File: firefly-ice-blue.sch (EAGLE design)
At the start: 119 parts, among them J1 USB-5PINMOLEX-47346, J2 CON-6SOCKET, U1 EFM32LG330F256, U10 STM6519, U11 TPS782XX, U12 TPS6208X, U13 NX3L1T53, U14 FDFMA2P029Z, U16 MEMORY-SPIWLBGA-8, U17 ADP151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

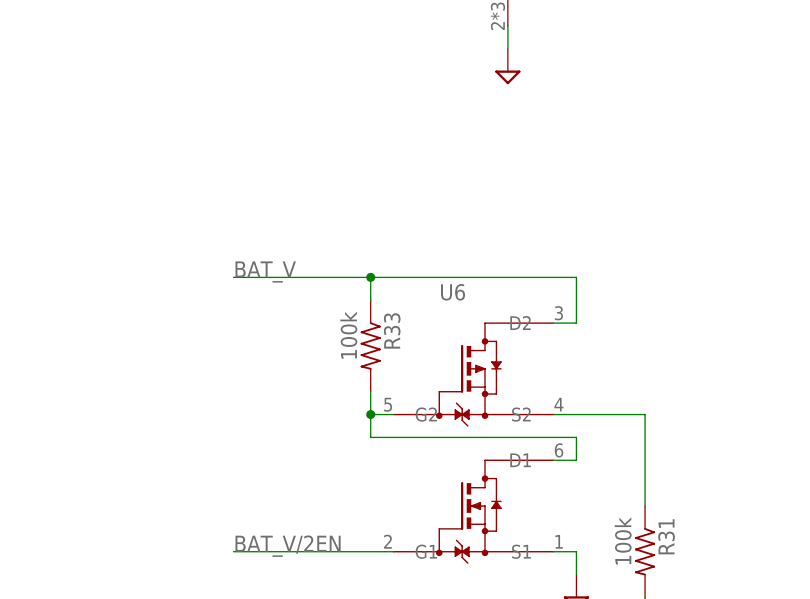
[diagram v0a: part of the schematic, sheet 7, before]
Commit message: fix reversed source/drain on p-channel mosfet of voltage sensing circuit
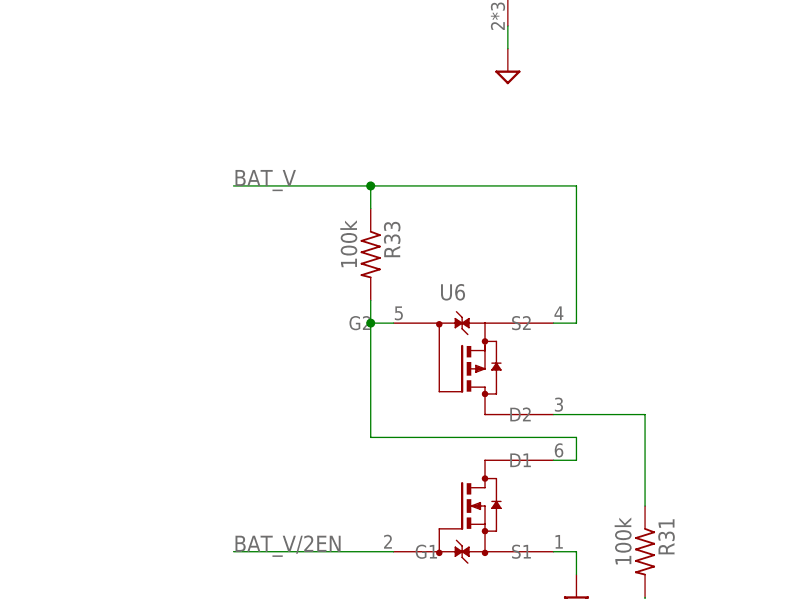
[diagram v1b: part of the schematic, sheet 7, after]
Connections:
- net BAT_V: now also U6.S2; no longer U6.D2
- net N$60: now also U6.D2; no longer U6.S2
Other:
- moved on the sheet: R33
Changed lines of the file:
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@@
 <attribute name="ORDERING-CODE" x="55.88" y="50.8" size="1.778" layer="96" display="off"/>
 </instance>
-<instance part="R33" gate="G$1" x="45.72" y="60.96" rot="R270">
-<attribute name="MANUFACTURER" x="45.72" y="60.96" size="1.778" layer="96" rot="R270" display="off"/>
-<attribute name="ORDERING-CODE" x="45.72" y="60.96" size="1.778" layer="96" rot="R270" display="off"/>
-<attribute name="VARIANTS" x="45.72" y="60.96" size="1.778" layer="96" rot="R270" display="off"/>
+<instance part="R33" gate="G$1" x="45.72" y="71.12" rot="R270">
+<attribute name="MANUFACTURER" x="45.72" y="71.12" size="1.778" layer="96" rot="R270" display="off"/>
+<attribute name="ORDERING-CODE" x="45.72" y="71.12" size="1.778" layer="96" rot="R270" display="off"/>
+<attribute name="VARIANTS" x="45.72" y="71.12" size="1.778" layer="96" rot="R270" display="off"/>
 </instance>
 <instance part="V93" gate="GND" x="68.58" y="33.02"/>
@@
 <segment>
 <pinref part="R33" gate="G$1" pin="1"/>
-<wire x1="45.72" y1="66.04" x2="45.72" y2="68.58" width="0.1524" layer="91"/>
-<wire x1="45.72" y1="68.58" x2="68.58" y2="68.58" width="0.1524" layer="91"/>
-<wire x1="68.58" y1="68.58" x2="68.58" y2="63.5" width="0.1524" layer="91"/>
-<pinref part="U6" gate="G$1" pin="D2"/>
+<wire x1="45.72" y1="76.2" x2="45.72" y2="78.74" width="0.1524" layer="91"/>
+<wire x1="45.72" y1="78.74" x2="68.58" y2="78.74" width="0.1524" layer="91"/>
+<wire x1="68.58" y1="78.74" x2="68.58" y2="63.5" width="0.1524" layer="91"/>
+<wire x1="30.48" y1="78.74" x2="45.72" y2="78.74" width="0.1524" layer="91"/>
+<junction x="45.72" y="78.74"/>
+<label x="30.48" y="78.74" size="1.778" layer="95"/>
+<pinref part="U6" gate="G$1" pin="S2"/>
 <wire x1="68.58" y1="63.5" x2="66.04" y2="63.5" width="0.1524" layer="91"/>
-<wire x1="30.48" y1="68.58" x2="45.72" y2="68.58" width="0.1524" layer="91"/>
-<junction x="45.72" y="68.58"/>
-<label x="30.48" y="68.58" size="1.778" layer="95"/>
 </segment>
 </net>
@@
 <segment>
 <pinref part="U6" gate="G$1" pin="G2"/>
-<wire x1="48.26" y1="53.34" x2="45.72" y2="53.34" width="0.1524" layer="91"/>
+<wire x1="48.26" y1="63.5" x2="45.72" y2="63.5" width="0.1524" layer="91"/>
 <pinref part="R33" gate="G$1" pin="2"/>
-<wire x1="45.72" y1="55.88" x2="45.72" y2="53.34" width="0.1524" layer="91"/>
+<wire x1="45.72" y1="66.04" x2="45.72" y2="63.5" width="0.1524" layer="91"/>
 <pinref part="U6" gate="G$1" pin="D1"/>
 <wire x1="66.04" y1="48.26" x2="68.58" y2="48.26" width="0.1524" layer="91"/>
 <wire x1="68.58" y1="48.26" x2="68.58" y2="50.8" width="0.1524" layer="91"/>
 <wire x1="68.58" y1="50.8" x2="45.72" y2="50.8" width="0.1524" layer="91"/>
-<wire x1="45.72" y1="50.8" x2="45.72" y2="53.34" width="0.1524" layer="91"/>
-<junction x="45.72" y="53.34"/>
+<wire x1="45.72" y1="50.8" x2="45.72" y2="63.5" width="0.1524" layer="91"/>
+<junction x="45.72" y="63.5"/>
 </segment>
 </net>
 <net name="N$60" class="0">
 <segment>
-<pinref part="U6" gate="G$1" pin="S2"/>
 <pinref part="R31" gate="G$1" pin="1"/>
+<wire x1="76.2" y1="53.34" x2="76.2" y2="43.18" width="0.1524" layer="91"/>
+<pinref part="U6" gate="G$1" pin="D2"/>
 <wire x1="66.04" y1="53.34" x2="76.2" y2="53.34" width="0.1524" layer="91"/>
-<wire x1="76.2" y1="53.34" x2="76.2" y2="43.18" width="0.1524" layer="91"/>
-</segment>
-</net>
+</segment>
+</net>

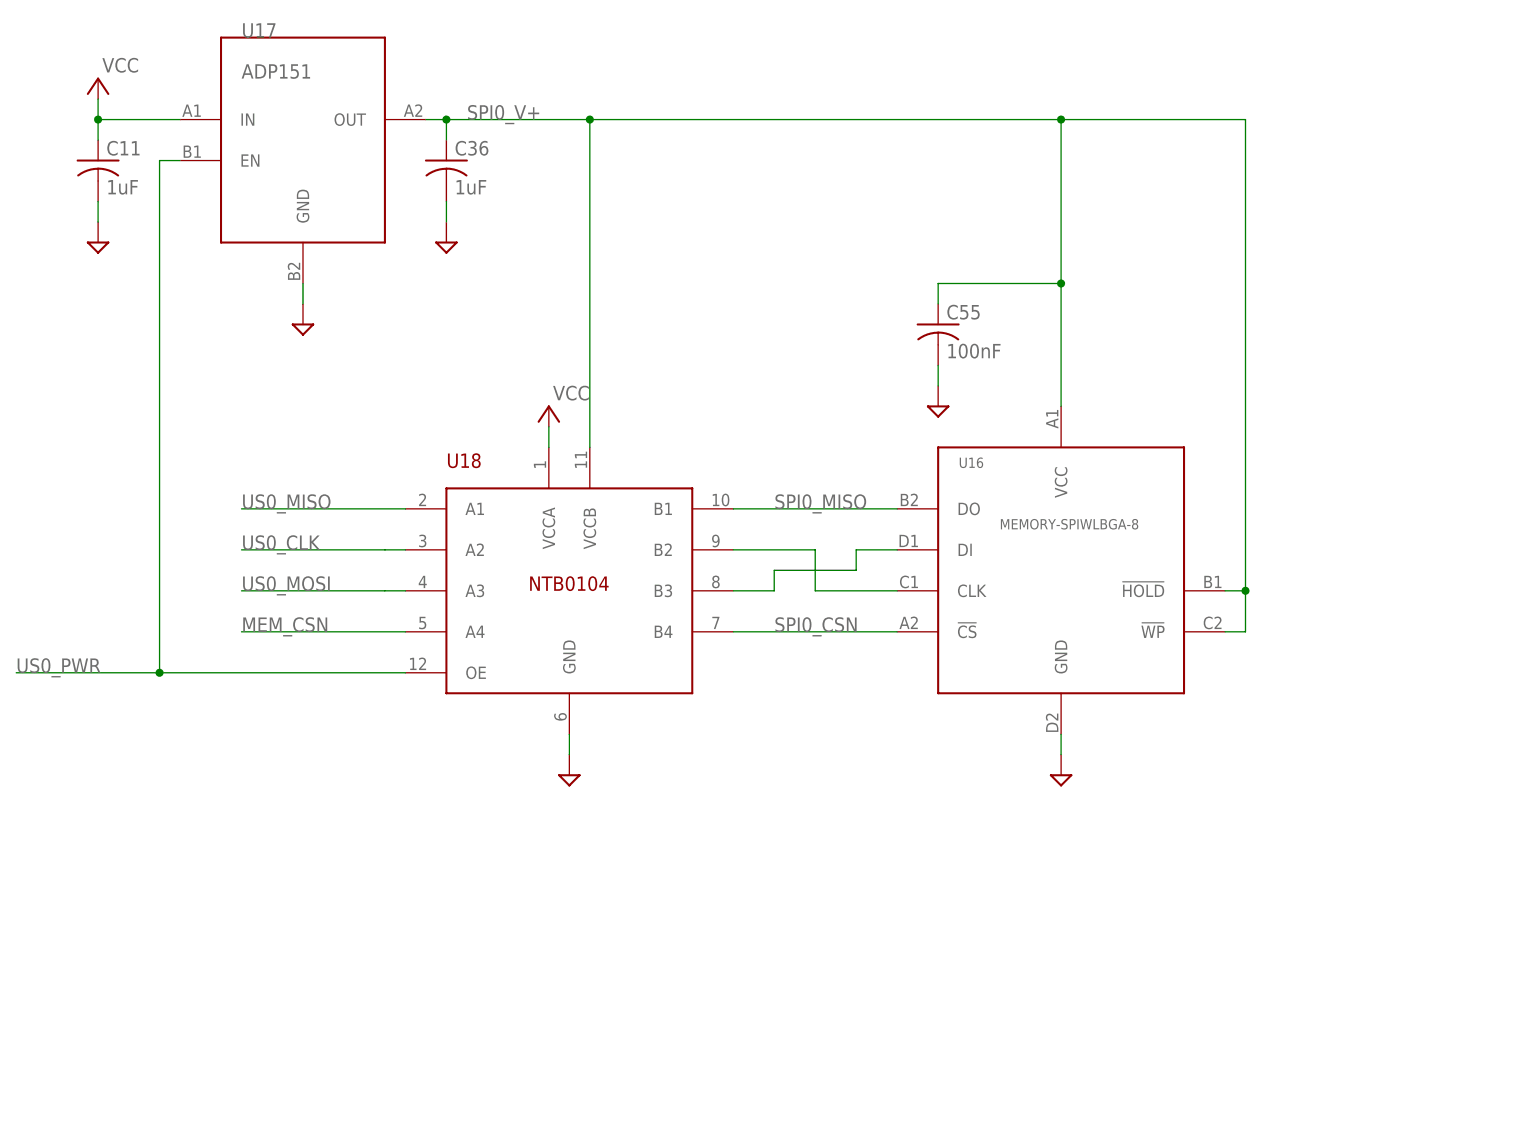
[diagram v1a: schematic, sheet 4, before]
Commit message: switch to splashproof USB connector; fix voltage translator connections (swap A and B sides); DFM improvements
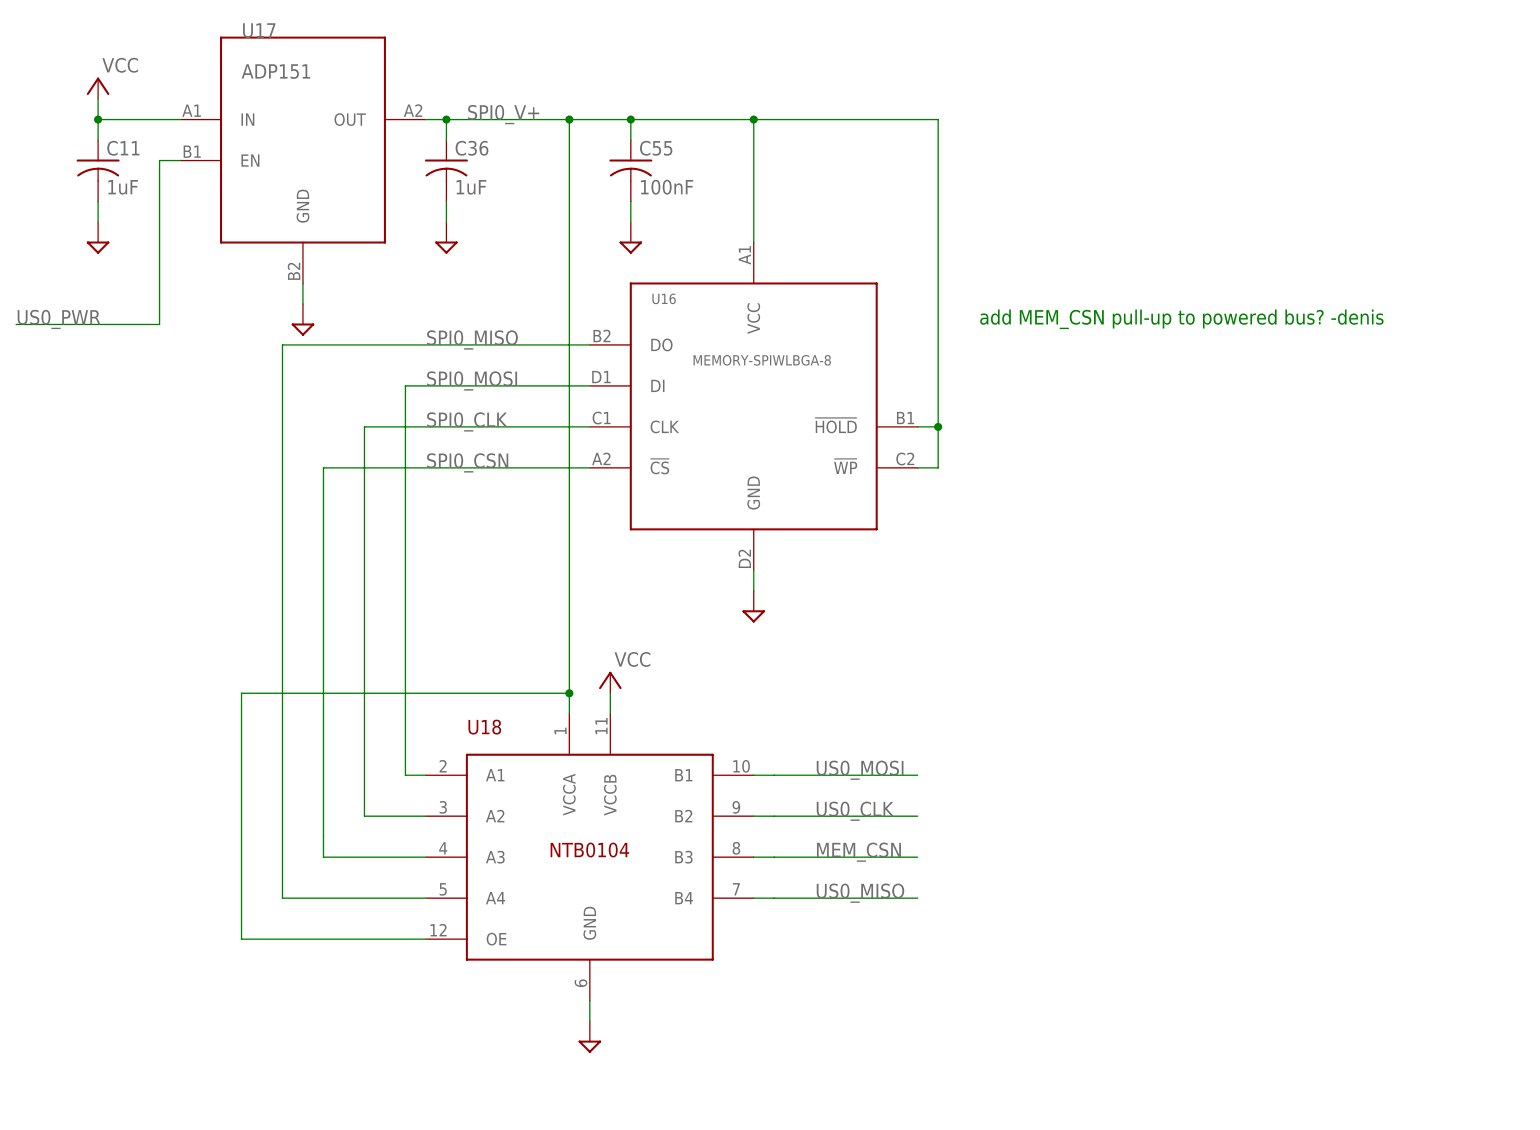
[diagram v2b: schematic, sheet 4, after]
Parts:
- J1: value USB-5PINMOLEX-47346 -> USB-5PINZX62WD1-B-5PC; device firefly:USB-5PINMOLEX-47346 -> firefly:USB-5PINZX62WD1-B-5PC; ALT-ORDERING-CODE 47346-1001 -> (none); MANUFACTURER Molex -> Hirose Electric Co Ltd; ORDERING-CODE 0473460001 -> ZX62WD1-B-5PC
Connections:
- removed net N$14: U16.CLK, U18.B2
- removed net N$18: U16.DI, U18.B3
- new net SPI0_CLK: U16.CLK, U18.A2
- new net SPI0_MOSI: U16.DI, U18.A1
- net MEM_CSN: now also U18.B3; no longer U18.A4
- net SPI0_CSN: now also U18.A3; no longer U18.B4
- net SPI0_MISO: now also U18.A4; no longer U18.B1
- net SPI0_V+: now also U18.OE, U18.VCCA; no longer U18.VCCB
- net US0_CLK: now also U18.B2; no longer U18.A2
- net US0_MISO: now also U18.B4; no longer U18.A1
- net US0_MOSI: now also U18.B1; no longer U18.A3
- net US0_PWR: no longer U18.OE
- net VCC: now also U18.VCCB; no longer U18.VCCA
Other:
- note added: "add MEM_CSN pull-up to powered bus? -denis"
- moved on the sheet: C55, U16, U18
